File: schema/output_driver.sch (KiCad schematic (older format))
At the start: 3 parts

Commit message: led driver MOS, correct opamp
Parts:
- removed Q?: Q_NMOS_DGS, symbol Q_NMOS_DGS
- added Q?: Q_NMOS_DGS, symbol Q_NMOS_DGS
- D?: symbol LED-RESCUE-IRemote -> LED
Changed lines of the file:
@@
 $EndComp
 $Comp
-L LED-RESCUE-IRemote D?
+L LED D?
 U 1 1 5910A491
 P 5750 3200
@@
 	0    -1   -1   0
 $EndComp
-Wire Wire Line
-	5750 3800 5750 3900
-Wire Wire Line
-	5750 2950 5750 3050
 $Comp
 L +5V #PWR?
@@
 $EndComp
 Wire Wire Line
+	5750 3800 5750 3900
+Wire Wire Line
+	5750 2950 5750 3050
+Wire Wire Line
 	5750 3350 5750 3500
 Wire Wire Line
 	5450 4100 5100 4100
+$Comp
+L Q_NMOS_DGS Q?
+U 1 1 5910A46B
+P 5650 4100
+F 0 "Q?" H 5850 4150 50  0000 L CNN
+F 1 "Q_NMOS_DGS" H 5850 4050 50  0000 L CNN
+F 2 "" H 5850 4200 50  0000 C CNN
+F 3 "" H 5650 4100 50  0000 C CNN
+	1    5650 4100
+	1    0    0    -1
+$EndComp
 $EndSCHEMATC

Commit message: fix values of decoder for 1ms period
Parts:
- removed Q?: Q_NMOS_DGS, symbol Q_NMOS_DGS
- added Q?: BC107B, symbol Q_NPN_EBC
- D?: value LED -> HLMPxxx
- R?: value R -> 150Ω
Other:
- note added: "V_CEsat = 0.25V"
- note added: "V_forward = 1.8V, 20mA"
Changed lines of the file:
@@
 DRIVER_INPUT
-$Comp
-L Q_NMOS_DGS Q?
-U 1 1 5910A46B
-P 5650 4100
-F 0 "Q?" H 5850 4150 50  0000 L CNN
-F 1 "Q_NMOS_DGS" H 5850 4050 50  0000 L CNN
-F 2 "" H 5850 4200 50  0000 C CNN
-F 3 "" H 5650 4100 50  0000 C CNN
-	1    5650 4100
-	1    0    0    -1
-$EndComp
 $Comp
 L LED D?
@@
 P 5750 3200
 F 0 "D?" H 5750 3300 50  0000 C CNN
-F 1 "LED" H 5750 3100 50  0000 C CNN
+F 1 "HLMPxxx" H 5750 3100 50  0000 C CNN
 F 2 "" H 5750 3200 50  0000 C CNN
 F 3 "" H 5750 3200 50  0000 C CNN
@@
 P 5750 3650
 F 0 "R?" V 5830 3650 50  0000 C CNN
-F 1 "R" V 5750 3650 50  0000 C CNN
+F 1 "150Ω" V 5650 3650 50  0000 C CNN
 F 2 "" V 5680 3650 50  0000 C CNN
 F 3 "" H 5750 3650 50  0000 C CNN
@@
 Wire Wire Line
 	5450 4100 5100 4100
+Text Notes 6000 3200 0    60   ~ 0
+V_forward = 1.8V, 20mA
 $Comp
-L Q_NMOS_DGS Q?
-U 1 1 5910A46B
+L Q_NPN_EBC Q?
+U 1 1 591420C1
 P 5650 4100
 F 0 "Q?" H 5850 4150 50  0000 L CNN
-F 1 "Q_NMOS_DGS" H 5850 4050 50  0000 L CNN
+F 1 "BC107B" H 5850 4050 50  0000 L CNN
 F 2 "" H 5850 4200 50  0000 C CNN
 F 3 "" H 5650 4100 50  0000 C CNN
@@
 	1    0    0    -1
 $EndComp
+Text Notes 6250 4100 0    60   ~ 0
+V_CEsat = 0.25V
 $EndSCHEMATC

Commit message: filter and comparator
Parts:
- gave numbers to parts that had none: 3
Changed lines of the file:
@@
 LIBS:contrib
 LIBS:valves
+LIBS:custom
 LIBS:IRemote-cache
 EELAYER 25 0
@@
 DRIVER_INPUT
 $Comp
-L LED D?
+L LED D3
 U 1 1 5910A491
 P 5750 3200
-F 0 "D?" H 5750 3300 50  0000 C CNN
+F 0 "D3" H 5750 3300 50  0000 C CNN
 F 1 "HLMPxxx" H 5750 3100 50  0000 C CNN
 F 2 "" H 5750 3200 50  0000 C CNN
@@
 $EndComp
 $Comp
-L +5V #PWR?
+L +5V #PWR27
 U 1 1 5910A522
 P 5750 2950
-F 0 "#PWR?" H 5750 2800 50  0001 C CNN
+F 0 "#PWR27" H 5750 2800 50  0001 C CNN
 F 1 "+5V" H 5750 3090 50  0000 C CNN
 F 2 "" H 5750 2950 50  0000 C CNN
@@
 $EndComp
 $Comp
-L GND #PWR?
+L GND #PWR28
 U 1 1 5910A53C
 P 5750 4300
-F 0 "#PWR?" H 5750 4050 50  0001 C CNN
+F 0 "#PWR28" H 5750 4050 50  0001 C CNN
 F 1 "GND" H 5750 4150 50  0000 C CNN
 F 2 "" H 5750 4300 50  0000 C CNN
@@
 $EndComp
 $Comp
-L R R?
+L R R22
 U 1 1 5910A571
 P 5750 3650
-F 0 "R?" V 5830 3650 50  0000 C CNN
+F 0 "R22" V 5830 3650 50  0000 C CNN
 F 1 "150Ω" V 5650 3650 50  0000 C CNN
 F 2 "" V 5680 3650 50  0000 C CNN
@@
 V_forward = 1.8V, 20mA
 $Comp
-L Q_NPN_EBC Q?
+L Q_NPN_EBC Q3
 U 1 1 591420C1
 P 5650 4100
-F 0 "Q?" H 5850 4150 50  0000 L CNN
+F 0 "Q3" H 5850 4150 50  0000 L CNN
 F 1 "BC107B" H 5850 4050 50  0000 L CNN
 F 2 "" H 5850 4200 50  0000 C CNN

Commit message: Reception: schmidt trigger
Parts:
- D3: symbol LED -> LED-RESCUE-IRemote
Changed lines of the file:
@@
 DRIVER_INPUT
 $Comp
-L LED D3
+L LED-RESCUE-IRemote D3
 U 1 1 5910A491
 P 5750 3200

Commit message: ouput driver
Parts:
- added C?: C, symbol C
- added R?: 150k, symbol R
- added U?: HEF4538, symbol HEF4538
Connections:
- wire segments 4 -> 23
- no-connect marks 0 -> 1
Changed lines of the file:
@@
 Text Notes 6250 4100 0    60   ~ 0
 V_CEsat = 0.25V
+$Comp
+L HEF4538 U?
+U 1 1 592FDAF4
+P 3000 2900
+F 0 "U?" H 3300 3300 60  0000 C CNN
+F 1 "HEF4538" H 3000 2900 60  0000 C CNN
+F 2 "" H 3100 2850 60  0001 C CNN
+F 3 "" H 3100 2850 60  0001 C CNN
+	1    3000 2900
+	1    0    0    -1
+$EndComp
+$Comp
+L C C?
+U 1 1 592FDBB7
+P 1400 2650
+F 0 "C?" H 1425 2750 50  0000 L CNN
+F 1 "C" H 1425 2550 50  0000 L CNN
+F 2 "" H 1438 2500 50  0000 C CNN
+F 3 "" H 1400 2650 50  0000 C CNN
+	1    1400 2650
+	1    0    0    -1
+$EndComp
+Wire Wire Line
+	1850 2650 2450 2650
+Wire Wire Line
+	1850 2450 1850 2650
+Wire Wire Line
+	2450 2750 1850 2750
+Wire Wire Line
+	1850 2750 1850 2850
+Wire Wire Line
+	1850 2850 1400 2850
+$Comp
+L R R?
+U 1 1 592FDD7D
+P 1400 2150
+F 0 "R?" V 1480 2150 50  0000 C CNN
+F 1 "150k" V 1400 2150 50  0000 C CNN
+F 2 "" V 1330 2150 50  0000 C CNN
+F 3 "" H 1400 2150 50  0000 C CNN
+	1    1400 2150
+	1    0    0    -1
+$EndComp
+Wire Wire Line
+	1400 2300 1400 2500
+Wire Wire Line
+	1400 2450 1850 2450
+Wire Wire Line
+	1400 2850 1400 2800
+Connection ~ 1400 2450
+Wire Wire Line
+	1400 2000 1400 1800
+$Comp
+L +5V #PWR?
+U 1 1 592FDE80
+P 1400 1800
+F 0 "#PWR?" H 1400 1650 50  0001 C CNN
+F 1 "+5V" H 1400 1940 50  0000 C CNN
+F 2 "" H 1400 1800 50  0000 C CNN
+F 3 "" H 1400 1800 50  0000 C CNN
+	1    1400 1800
+	1    0    0    -1
+$EndComp
+$Comp
+L +5V #PWR?
+U 1 1 592FE41E
+P 3800 2000
+F 0 "#PWR?" H 3800 1850 50  0001 C CNN
+F 1 "+5V" H 3800 2140 50  0000 C CNN
+F 2 "" H 3800 2000 50  0000 C CNN
+F 3 "" H 3800 2000 50  0000 C CNN
+	1    3800 2000
+	1    0    0    -1
+$EndComp
+Wire Wire Line
+	3600 2650 3800 2650
+Wire Wire Line
+	3800 2650 3800 2000
+Wire Wire Line
+	3600 2850 3950 2850
+Wire Wire Line
+	3950 2850 3950 4900
+Wire Wire Line
+	2450 3000 750  3000
+Wire Wire Line
+	2450 2900 2400 2900
+Wire Wire Line
+	2400 2300 2400 3150
+$Comp
+L +5V #PWR?
+U 1 1 592FE666
+P 2400 2300
+F 0 "#PWR?" H 2400 2150 50  0001 C CNN
+F 1 "+5V" H 2400 2440 50  0000 C CNN
+F 2 "" H 2400 2300 50  0000 C CNN
+F 3 "" H 2400 2300 50  0000 C CNN
+	1    2400 2300
+	1    0    0    -1
+$EndComp
+Wire Wire Line
+	2400 3150 2450 3150
+Connection ~ 2400 2900
+$Comp
+L GND #PWR?
+U 1 1 592FE7B3
+P 3750 3400
+F 0 "#PWR?" H 3750 3150 50  0001 C CNN
+F 1 "GND" H 3750 3250 50  0000 C CNN
+F 2 "" H 3750 3400 50  0000 C CNN
+F 3 "" H 3750 3400 50  0000 C CNN
+	1    3750 3400
+	1    0    0    -1
+$EndComp
+Wire Wire Line
+	3600 3150 3750 3150
+Wire Wire Line
+	3750 3150 3750 3400
+NoConn ~ 3600 2950
 $EndSCHEMATC

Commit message: reannotate schema
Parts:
- gave numbers to parts that had none: 3
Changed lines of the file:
@@
 $Descr A4 11693 8268
 encoding utf-8
-Sheet 5 6
+Sheet 4 6
 Title ""
 Date ""
@@
 $EndComp
 $Comp
-L +5V #PWR27
+L +5V #PWR24
 U 1 1 5910A522
 P 5750 2950
-F 0 "#PWR27" H 5750 2800 50  0001 C CNN
+F 0 "#PWR24" H 5750 2800 50  0001 C CNN
 F 1 "+5V" H 5750 3090 50  0000 C CNN
 F 2 "" H 5750 2950 50  0000 C CNN
@@
 $EndComp
 $Comp
-L GND #PWR28
+L GND #PWR25
 U 1 1 5910A53C
 P 5750 4300
-F 0 "#PWR28" H 5750 4050 50  0001 C CNN
+F 0 "#PWR25" H 5750 4050 50  0001 C CNN
 F 1 "GND" H 5750 4150 50  0000 C CNN
 F 2 "" H 5750 4300 50  0000 C CNN
@@
 V_CEsat = 0.25V
 $Comp
-L HEF4538 U?
+L HEF4538 U4
 U 1 1 592FDAF4
 P 3000 2900
-F 0 "U?" H 3300 3300 60  0000 C CNN
+F 0 "U4" H 3300 3300 60  0000 C CNN
 F 1 "HEF4538" H 3000 2900 60  0000 C CNN
 F 2 "" H 3100 2850 60  0001 C CNN
@@
 $EndComp
 $Comp
-L C C?
+L C C6
 U 1 1 592FDBB7
 P 1400 2650
-F 0 "C?" H 1425 2750 50  0000 L CNN
+F 0 "C6" H 1425 2750 50  0000 L CNN
 F 1 "C" H 1425 2550 50  0000 L CNN
 F 2 "" H 1438 2500 50  0000 C CNN
@@
 	1850 2850 1400 2850
 $Comp
-L R R?
+L R R12
 U 1 1 592FDD7D
 P 1400 2150
-F 0 "R?" V 1480 2150 50  0000 C CNN
+F 0 "R12" V 1480 2150 50  0000 C CNN
 F 1 "150k" V 1400 2150 50  0000 C CNN
 F 2 "" V 1330 2150 50  0000 C CNN
@@
 	1400 2000 1400 1800
 $Comp
-L +5V #PWR?
+L +5V #PWR20
 U 1 1 592FDE80
 P 1400 1800
-F 0 "#PWR?" H 1400 1650 50  0001 C CNN
+F 0 "#PWR20" H 1400 1650 50  0001 C CNN
 F 1 "+5V" H 1400 1940 50  0000 C CNN
 F 2 "" H 1400 1800 50  0000 C CNN
@@
 $EndComp
 $Comp
-L +5V #PWR?
+L +5V #PWR23
 U 1 1 592FE41E
 P 3800 2000
-F 0 "#PWR?" H 3800 1850 50  0001 C CNN
+F 0 "#PWR23" H 3800 1850 50  0001 C CNN
 F 1 "+5V" H 3800 2140 50  0000 C CNN
 F 2 "" H 3800 2000 50  0000 C CNN
@@
 	2400 2300 2400 3150
 $Comp
-L +5V #PWR?
+L +5V #PWR21
 U 1 1 592FE666
 P 2400 2300
-F 0 "#PWR?" H 2400 2150 50  0001 C CNN
+F 0 "#PWR21" H 2400 2150 50  0001 C CNN
 F 1 "+5V" H 2400 2440 50  0000 C CNN
 F 2 "" H 2400 2300 50  0000 C CNN
@@
 Connection ~ 2400 2900
 $Comp
-L GND #PWR?
+L GND #PWR22
 U 1 1 592FE7B3
 P 3750 3400
-F 0 "#PWR?" H 3750 3150 50  0001 C CNN
+F 0 "#PWR22" H 3750 3150 50  0001 C CNN
 F 1 "GND" H 3750 3250 50  0000 C CNN
 F 2 "" H 3750 3400 50  0000 C CNN

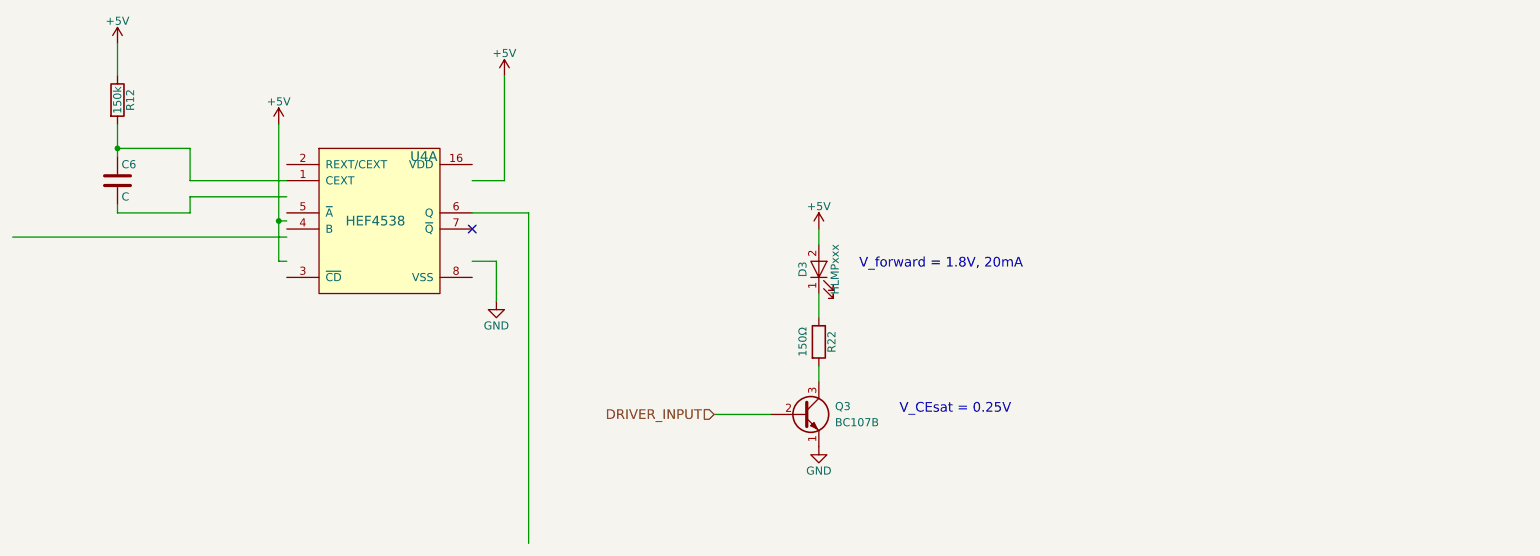
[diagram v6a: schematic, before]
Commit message: output driver schema
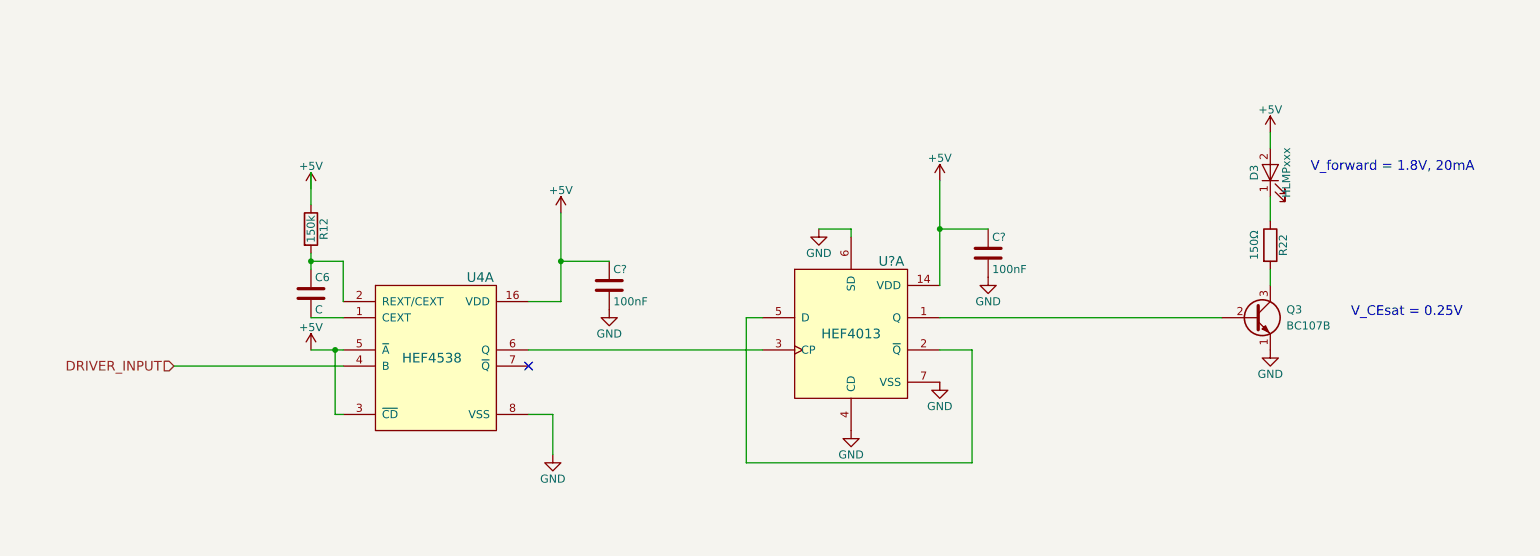
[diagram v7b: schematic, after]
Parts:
- added C? (x2): 100nF, symbol C
- added U?: HEF4013, symbol HEF4013
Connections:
- wire segments 23 -> 28
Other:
- moved on the sheet: C6, D3, Q3, R12, R22, U4A

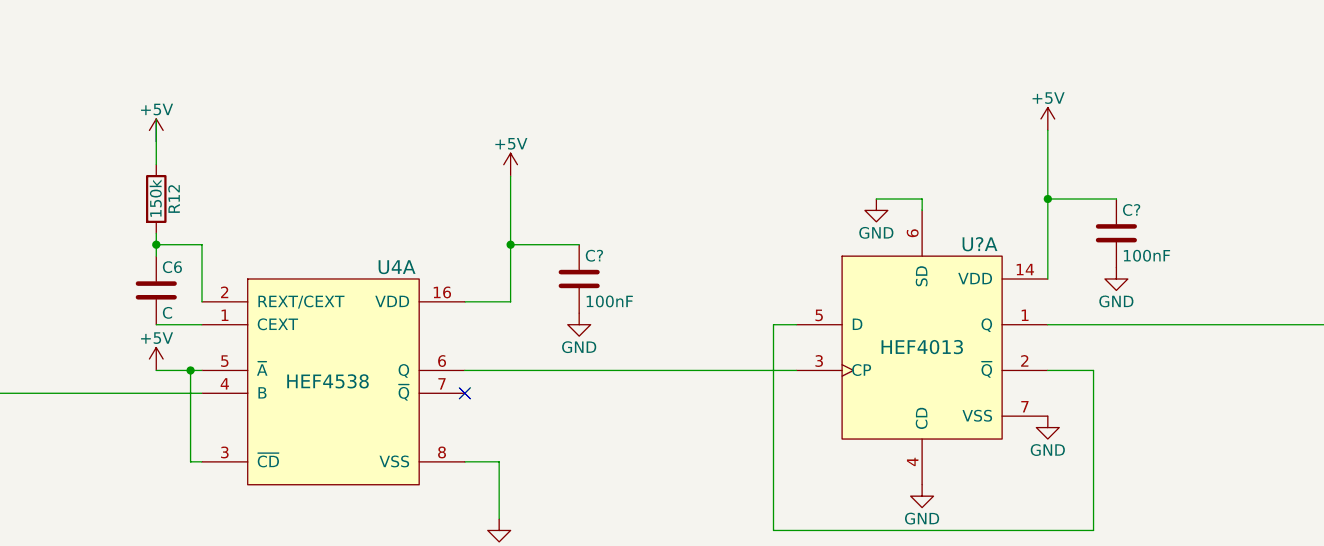
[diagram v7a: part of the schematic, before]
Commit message: Schematic done
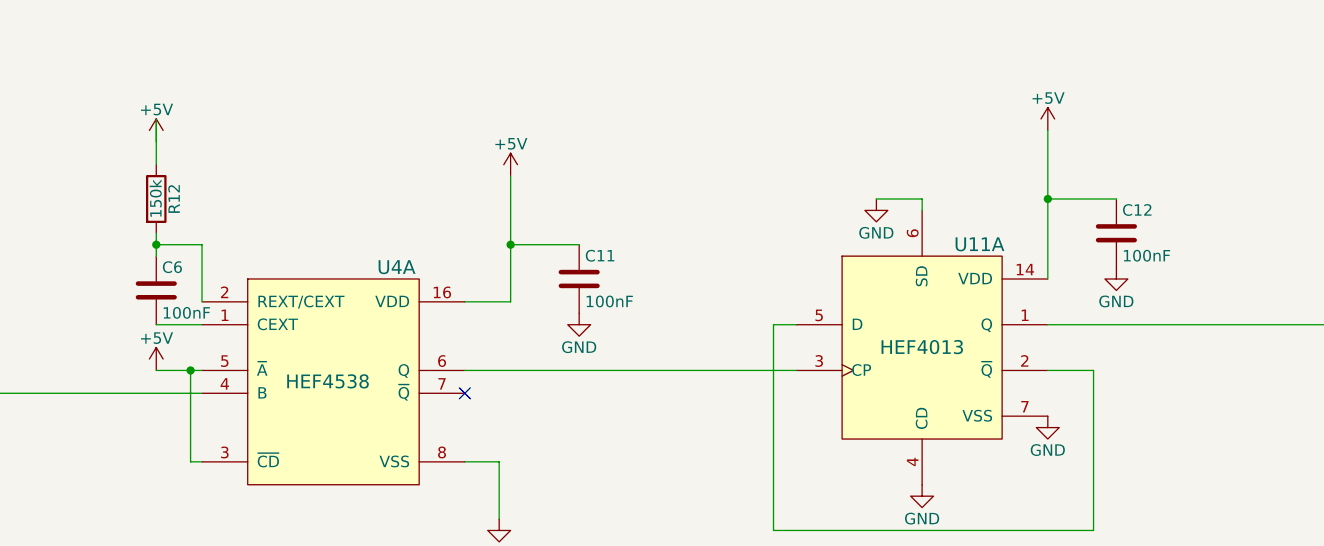
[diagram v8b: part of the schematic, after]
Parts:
- C6: value C -> 100nF
- gave numbers to parts that had none: 3
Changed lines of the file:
@@
 encoding utf-8
 Sheet 4 6
-Title ""
+Title "Output Driver"
 Date ""
 Rev ""
@@
 $EndComp
 $Comp
-L +5V #PWR24
+L +5V #PWR32
 U 1 1 5910A522
 P 8550 2350
-F 0 "#PWR24" H 8550 2200 50  0001 C CNN
+F 0 "#PWR32" H 8550 2200 50  0001 C CNN
 F 1 "+5V" H 8550 2490 50  0000 C CNN
 F 2 "" H 8550 2350 50  0000 C CNN
@@
 $EndComp
 $Comp
-L GND #PWR25
+L GND #PWR33
 U 1 1 5910A53C
 P 8550 3700
-F 0 "#PWR25" H 8550 3450 50  0001 C CNN
+F 0 "#PWR33" H 8550 3450 50  0001 C CNN
 F 1 "GND" H 8550 3550 50  0000 C CNN
 F 2 "" H 8550 3700 50  0000 C CNN
@@
 P 2600 3350
 F 0 "C6" H 2625 3450 50  0000 L CNN
-F 1 "C" H 2625 3250 50  0000 L CNN
+F 1 "100nF" H 2625 3250 50  0000 L CNN
 F 2 "" H 2638 3200 50  0000 C CNN
 F 3 "" H 2600 3350 50  0000 C CNN
@@
 	2600 2800 2600 2600
 $Comp
-L +5V #PWR20
+L +5V #PWR22
 U 1 1 592FDE80
 P 2600 2700
-F 0 "#PWR20" H 2600 2550 50  0001 C CNN
+F 0 "#PWR22" H 2600 2550 50  0001 C CNN
 F 1 "+5V" H 2600 2840 50  0000 C CNN
 F 2 "" H 2600 2700 50  0000 C CNN
@@
 $EndComp
 $Comp
-L +5V #PWR23
+L +5V #PWR25
 U 1 1 592FE41E
 P 4150 2850
-F 0 "#PWR23" H 4150 2700 50  0001 C CNN
+F 0 "#PWR25" H 4150 2700 50  0001 C CNN
 F 1 "+5V" H 4150 2990 50  0000 C CNN
 F 2 "" H 4150 2850 50  0000 C CNN
@@
 	2800 3800 1750 3800
 $Comp
-L +5V #PWR21
+L +5V #PWR23
 U 1 1 592FE666
 P 2600 3700
-F 0 "#PWR21" H 2600 3550 50  0001 C CNN
+F 0 "#PWR23" H 2600 3550 50  0001 C CNN
 F 1 "+5V" H 2600 3840 50  0000 C CNN
 F 2 "" H 2600 3700 50  0000 C CNN
@@
 $EndComp
 $Comp
-L GND #PWR22
+L GND #PWR24
 U 1 1 592FE7B3
 P 4100 4350
-F 0 "#PWR22" H 4100 4100 50  0001 C CNN
+F 0 "#PWR24" H 4100 4100 50  0001 C CNN
 F 1 "GND" H 4100 4200 50  0000 C CNN
 F 2 "" H 4100 4350 50  0000 C CNN
@@
 NoConn ~ 3950 3800
 $Comp
-L HEF4013 U?
+L HEF4013 U11
 U 1 1 593C8AEA
 P 5950 3600
-F 0 "U?" H 6200 4050 60  0000 C CNN
+F 0 "U11" H 6200 4050 60  0000 C CNN
 F 1 "HEF4013" H 5950 3600 60  0000 C CNN
 F 2 "" H 6000 3550 60  0001 C CNN
@@
 	6700 3700 6500 3700
 $Comp
-L C C?
+L C C11
 U 1 1 593C93B8
 P 4450 3300
-F 0 "C?" H 4475 3400 50  0000 L CNN
+F 0 "C11" H 4475 3400 50  0000 L CNN
 F 1 "100nF" H 4475 3200 50  0000 L CNN
 F 2 "" H 4488 3150 50  0000 C CNN
@@
 Connection ~ 4150 3150
 $Comp
-L GND #PWR?
+L GND #PWR26
 U 1 1 593C9421
 P 4450 3450
-F 0 "#PWR?" H 4450 3200 50  0001 C CNN
+F 0 "#PWR26" H 4450 3200 50  0001 C CNN
 F 1 "GND" H 4450 3300 50  0000 C CNN
 F 2 "" H 4450 3450 50  0000 C CNN
@@
 $EndComp
 $Comp
-L C C?
+L C C12
 U 1 1 593C944B
 P 6800 3100
-F 0 "C?" H 6825 3200 50  0000 L CNN
+F 0 "C12" H 6825 3200 50  0000 L CNN
 F 1 "100nF" H 6825 3000 50  0000 L CNN
 F 2 "" H 6838 2950 50  0000 C CNN
@@
 	5300 3500 5300 4400
 $Comp
-L GND #PWR?
+L GND #PWR30
 U 1 1 593C9562
 P 6500 3900
-F 0 "#PWR?" H 6500 3650 50  0001 C CNN
+F 0 "#PWR30" H 6500 3650 50  0001 C CNN
 F 1 "GND" H 6500 3750 50  0000 C CNN
 F 2 "" H 6500 3900 50  0000 C CNN
@@
 $EndComp
 $Comp
-L GND #PWR?
+L GND #PWR31
 U 1 1 593C9588
 P 6800 3250
-F 0 "#PWR?" H 6800 3000 50  0001 C CNN
+F 0 "#PWR31" H 6800 3000 50  0001 C CNN
 F 1 "GND" H 6800 3100 50  0000 C CNN
 F 2 "" H 6800 3250 50  0000 C CNN
@@
 Connection ~ 6500 2950
 $Comp
-L +5V #PWR?
+L +5V #PWR29
 U 1 1 593C9631
 P 6500 2650
-F 0 "#PWR?" H 6500 2500 50  0001 C CNN
+F 0 "#PWR29" H 6500 2500 50  0001 C CNN
 F 1 "+5V" H 6500 2790 50  0000 C CNN
 F 2 "" H 6500 2650 50  0000 C CNN
@@
 Connection ~ 2750 3700
 $Comp
-L GND #PWR?
+L GND #PWR28
 U 1 1 593CBF84
 P 5950 4200
-F 0 "#PWR?" H 5950 3950 50  0001 C CNN
+F 0 "#PWR28" H 5950 3950 50  0001 C CNN
 F 1 "GND" H 5950 4050 50  0000 C CNN
 F 2 "" H 5950 4200 50  0000 C CNN
@@
 $EndComp
 $Comp
-L GND #PWR?
+L GND #PWR27
 U 1 1 593CC00A
 P 5750 2950
-F 0 "#PWR?" H 5750 2700 50  0001 C CNN
+F 0 "#PWR27" H 5750 2700 50  0001 C CNN
 F 1 "GND" H 5750 2800 50  0000 C CNN
 F 2 "" H 5750 2950 50  0000 C CNN
